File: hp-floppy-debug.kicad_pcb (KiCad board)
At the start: 2 copper layers, 147 x 101.6 mm, 75 parts, among them J1 34-Pin HD Floppy Interface, J2 34-Pin HD Floppy Interface, J3 34-Pin HD Floppy Interface, J4 Conn_01x04, J5 Conn_01x05, J6 Conn_01x04, J7 Conn_02x02_Odd_Even, M1 3.5in_HDD_Mount, SW1 RotaryEncoder_Switch, U1 74LS09, U2 74LS09, U3 74LS09, U4 MAX232

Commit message: review changes
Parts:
- removed REF**: Logo, Logo:Logo
- added J8: Conn_01x05, Connector_PinHeader_2.54mm:PinHeader_1x05_P2.54mm_Vertical, F.Cu at (41.3, 112.4)
- added JP36: SolderJumper_2_Bridged, Jumper:SolderJumper-2_P1.3mm_Bridged_RoundedPad1.0x1.5mm, B.Cu at (166.4, 109.9)
- added JP37: SolderJumper_2_Bridged, Jumper:SolderJumper-2_P1.3mm_Bridged_RoundedPad1.0x1.5mm, B.Cu at (163.8, 109.9)
- added JP38: SolderJumper_2_Bridged, Jumper:SolderJumper-2_P1.3mm_Bridged_RoundedPad1.0x1.5mm, B.Cu at (166.4, 118.7)
- moved J5 6.30 mm to (41.3, 101.0)
- moved SW1 6.30 mm to (43.9, 95.5)
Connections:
- A1 pad 10: unconnected-(A1-Pad10) -> Net-(A1-Pad10)
- A1 pad 21: unconnected-(A1-Pad21) -> Net-(A1-Pad21)
- A1 pad 22: unconnected-(A1-Pad22) -> Net-(A1-Pad22)
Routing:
- net /DISK_CHANGE: track 67.6 -> 182.4 mm
- net /STEP: track 164.3 -> 266.7 mm
- net /DIR: track 160.8 -> 257.4 mm
- net (no net): track 0.00 -> 33.1 mm
- net GND: track 529.3 -> 510.7 mm, vias 3 -> 4
- net Net-(A1-Pad13): track 185.4 -> 167.1 mm, vias 0 -> 1
- net Net-(A1-Pad12): track 164.7 -> 159.1 mm, vias 0 -> 1
- net Net-(A1-Pad11): track 162.7 -> 157.8 mm, vias 0 -> 1
- net Net-(A1-Pad22): track 0.00 -> 2.53 mm
- net Net-(A1-Pad21): track 0.00 -> 2.53 mm
- net Net-(A1-Pad10): track 0.00 -> 2.52 mm

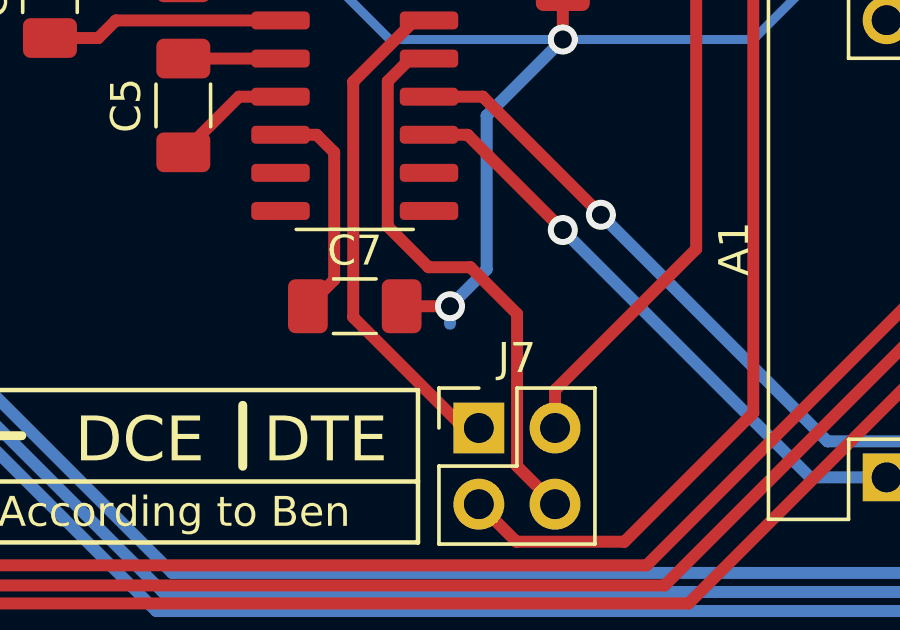
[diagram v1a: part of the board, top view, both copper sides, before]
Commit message: Remove unconnected trace
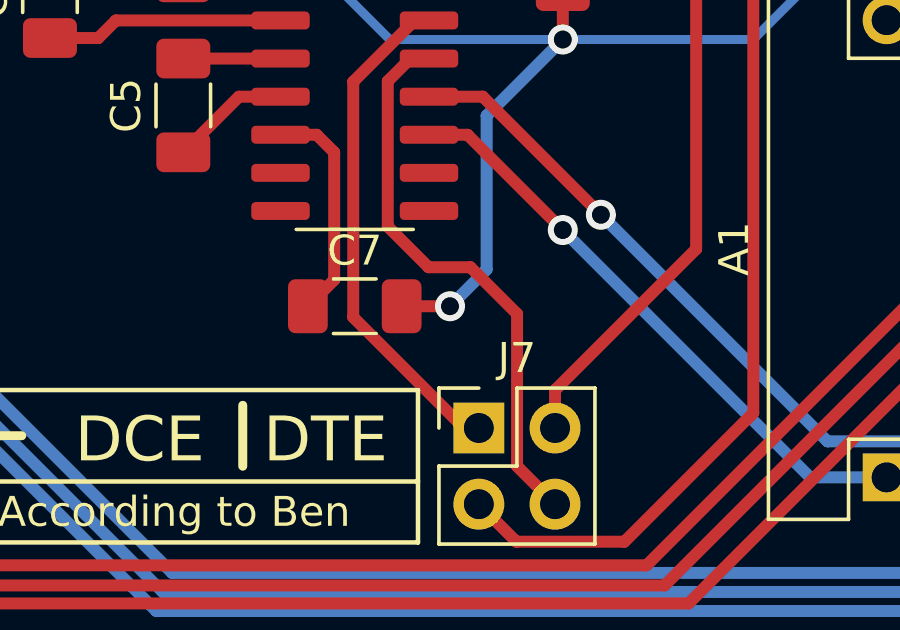
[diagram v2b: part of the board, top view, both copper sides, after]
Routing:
- net GND: track 510.7 -> 510.1 mm
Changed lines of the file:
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@@
   (segment (start 111.765 85.085) (end 111.765 81.285) (width 0.3) (layer "B.Cu") (net 2))
   (segment (start 63.5 86.36) (end 63.51 86.35) (width 0.3) (layer "B.Cu") (net 2))
-  (segment (start 128.955 116.205) (end 128.955 116.79) (width 0.4) (layer "B.Cu") (net 2))
   (segment (start 126.95 107.315) (end 120.015 100.38) (width 0.3) (layer "B.Cu") (net 2))
   (segment (start 132.715 107.315) (end 130.175 109.855) (width 0.4) (layer "B.Cu") (net 2))
